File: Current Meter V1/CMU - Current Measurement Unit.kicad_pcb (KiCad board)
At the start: 2 copper layers, 35 parts, among them J401 I2C OLED Display Connector, J501 Connector, U201 MCP6002-xSN, U202 MCP6002-xSN

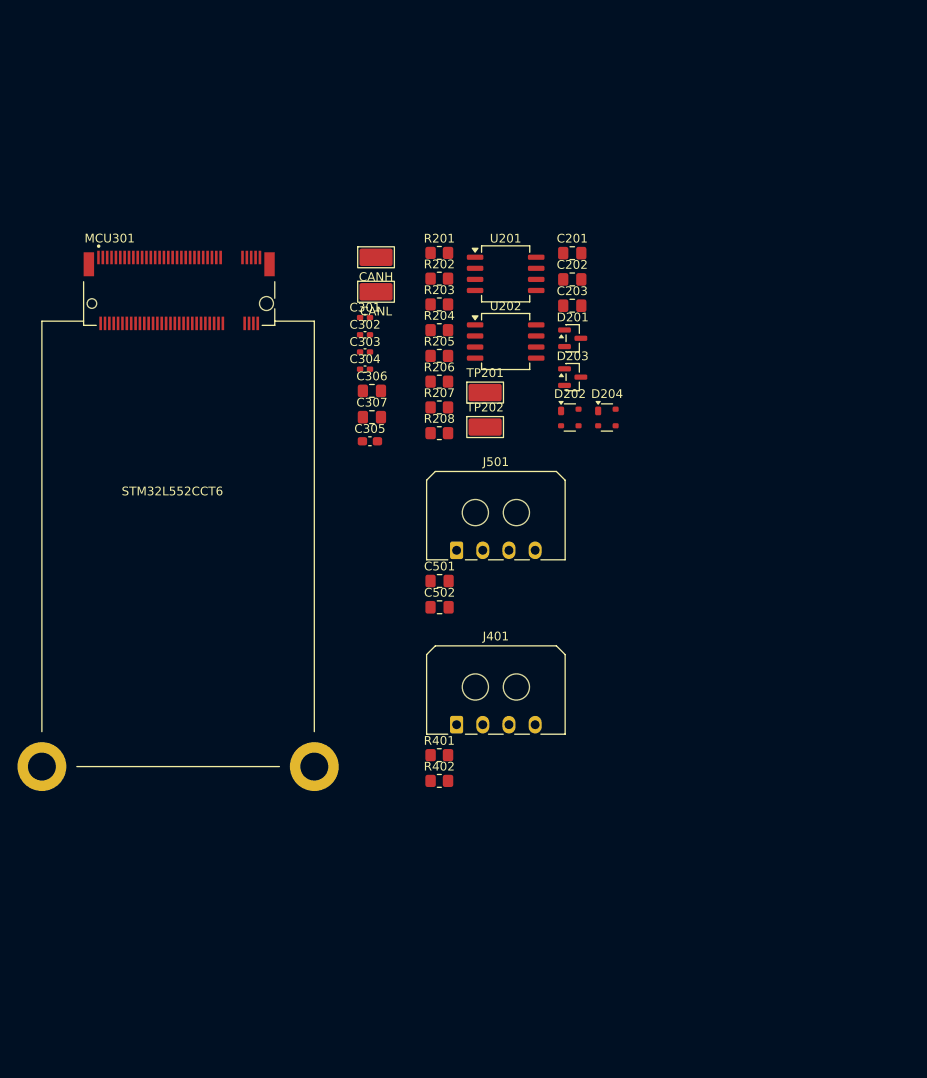
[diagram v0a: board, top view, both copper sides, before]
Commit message: updates
started layout
deleted usb
fully updated op amp footprints
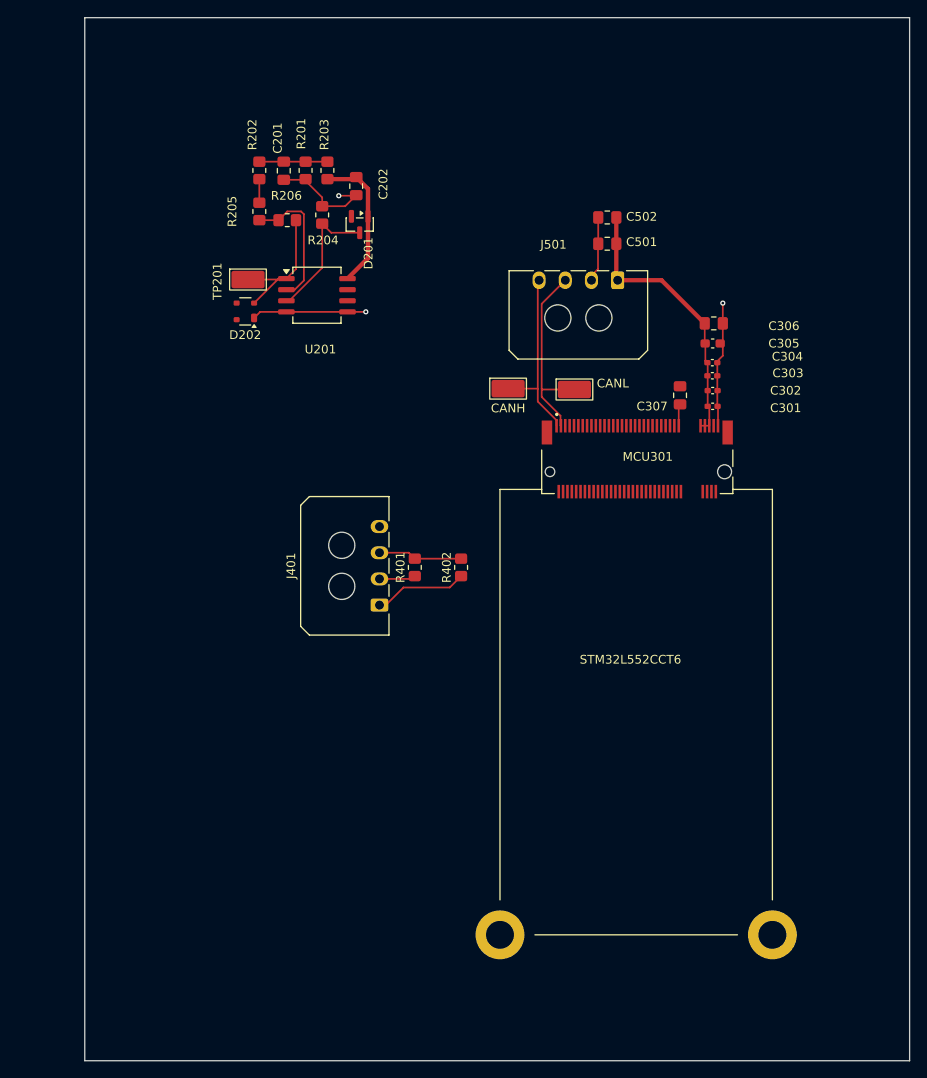
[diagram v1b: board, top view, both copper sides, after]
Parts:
- removed C203: 100n, Capacitor_SMD:C_0805_2012Metric_Pad1.18x1.45mm_HandSolder
- removed D203: BAT54A, Package_TO_SOT_SMD:SOT-23
- removed D204: PRTR5V0U2X, Package_TO_SOT_SMD:SOT-143
- removed R207: 8.2k, Resistor_SMD:R_0805_2012Metric_Pad1.20x1.40mm_HandSolder
- removed R208: 22k, Resistor_SMD:R_0805_2012Metric_Pad1.20x1.40mm_HandSolder
- removed TP202: SMD Test Point, TestPoint:TestPoint_Keystone_5019_Miniature
- removed U202: MCP6002-xSN, Package_SO:SOIC-8_5.3x6.2mm_P1.27mm
- moved MCU301 55.9 mm to (166.2, 92.5)
- moved C502 48.6 mm to (162.8, 64.9), turned to 180 degrees
- moved C501 43.2 mm to (162.8, 67.9), turned to 180 degrees
- moved C301 41.1 mm to (174.8, 86.5)
- moved C305 40.8 mm to (174.8, 79.3)
- moved C302 40.3 mm to (174.8, 84.7)
- moved C306 39.9 mm to (175.0, 77.0)
- moved C303 39.9 mm to (174.8, 83.0)
- moved C304 39.8 mm to (174.8, 81.5)
- moved D202 39.1 mm to (121.3, 75.7), turned to 180 degrees
- moved J501 36.0 mm to (163.9, 72.1), turned to 180 degrees
- moved C307 35.4 mm to (171.1, 85.3), turned to -90 degrees
- moved C201 34.4 mm to (125.7, 59.5), turned to 90 degrees
- moved TP201 30.1 mm to (121.6, 72.0)
- moved D201 27.7 mm to (134.4, 65.7), turned to -90 degrees
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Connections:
- MCU301 pad 45: /opamp/Vout=0.40 Min, 3.278 Max -> /microcontroller/curr_sig
- R205 pad 2: Net-(U202A--) -> Net-(U201A--)
- R206 pad 1: Net-(U202A--) -> Net-(U201A--)
- U201 pad 1: Net-(U201A--) -> /opamp/Gain=0.833, 1.67 (0-3.3)
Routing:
- net GND: track 0.00 -> 50.3 mm, vias 0 -> 3
- net /connector/+5_V: track 0.00 -> 32.2 mm
- net /connector/CAN-: track 0.00 -> 22.5 mm
- net /connector/CAN+: track 0.00 -> 21.0 mm
- net +5V: track 0.00 -> 16.6 mm
- net /opamp/Gain=0.833, 1.67 (0-3.3): track 0.00 -> 16.5 mm
- net Net-(U201A--): track 0.00 -> 15.7 mm
- net /opamp/2.5V, 0.55V-4.5V: track 0.00 -> 15.5 mm
- net /display/I2C_SDA: track 0.00 -> 10.7 mm
- net +3V3: track 0.00 -> 9.63 mm
- net /opamp/0.54V: track 0.00 -> 7.80 mm
- net /display/I2C_SCL: track 0.00 -> 4.18 mm
- net Net-(R202-Pad1): track 0.00 -> 2.70 mm
- added copper zone on In1.Cu, net +5V
- added copper zone on In2.Cu, net GND
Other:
- board outline added: 94.5 x 119.5 mm
- copper layers 2 -> 4

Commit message: buck converter
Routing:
- net GND: track 50.3 -> 50.8 mm, vias 3 -> 5
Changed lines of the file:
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@@
+	)
+	(segment
+		(start 174.95 88.75)
+		(end 175.45 88.75)
+		(width 0.2)
+		(layer "F.Cu")
+		(net 1)
 	)
 	(segment
@@
 		(size 0.6)
 		(drill 0.3)
+		(layers "F.Cu" "B.Cu")
+		(free yes)
+		(net 1)
+	)
+	(via
+		(at 164.2 90.2)
+		(size 0.6)
+		(drill 0.3)
+		(layers "F.Cu" "B.Cu")
+		(free yes)
+		(net 1)
+	)
+	(via
+		(at 174.7 90.5)
+		(size 0.6)
+		(drill 0.3)

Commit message: layup updated
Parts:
- added C601: 10u, Capacitor_SMD:C_0603_1608Metric_Pad1.08x0.95mm_HandSolder, F.Cu at (131.5, 117.9)
- added C602: 10n, Capacitor_SMD:C_0603_1608Metric_Pad1.08x0.95mm_HandSolder, F.Cu at (127.4, 122.8)
- added C603: 220u, Capacitor_THT:CP_Radial_D8.0mm_P3.50mm, F.Cu at (136.1, 134.2)
- added D601: B340, Diode_SMD:D_SMC, F.Cu at (122.8, 123.8)
- added L601: 15u, bfr_inductors:CDRH104RNP-150NC, F.Cu at (126.9, 134.6)
- added R601: 10k, Resistor_SMD:R_0805_2012Metric_Pad1.20x1.40mm_HandSolder, F.Cu at (139.3, 128.2)
- added R602: 3.3k, Resistor_SMD:R_0805_2012Metric_Pad1.20x1.40mm_HandSolder, F.Cu at (139.2, 125.2)
- added SW601: SW_DIP_x01, Button_Switch_SMD:SW_DIP_SPSTx01_Slide_6.7x4.1mm_W6.73mm_P2.54mm_LowProfile_JPin, F.Cu at (138.0, 118.9)
- added U601: TPS5430DDAR, Package_SO:TI_SO-PowerPAD-8_ThermalVias, F.Cu at (131.3, 122.9)
- moved R202 49.8 mm to (136.6, 107.4), turned to -90 degrees
- moved C201 48.5 mm to (133.8, 107.4), turned to -90 degrees
- moved R201 48.0 mm to (131.3, 107.4), turned to -90 degrees
- moved R203 48.0 mm to (128.8, 107.4), turned to 90 degrees
- moved C202 45.1 mm to (125.5, 105.6), turned to 90 degrees
- moved R205 40.9 mm to (136.6, 102.7), turned to 90 degrees
- moved R204 37.7 mm to (129.4, 102.3), turned to 90 degrees
- moved R206 37.3 mm to (133.4, 101.7), turned to 180 degrees
- moved D201 36.7 mm to (125.1, 101.2), turned to 90 degrees
- moved J401 30.1 mm to (129.0, 80.2)
- moved TP201 28.1 mm to (137.9, 94.9), turned to 180 degrees
- moved C502 26.4 mm to (138.3, 74.9), turned to -90 degrees
- moved D202 23.0 mm to (138.2, 91.3), turned to 0 degrees
- moved C501 22.6 mm to (141.3, 74.9), turned to -90 degrees
- moved R401 20.2 mm to (143.8, 85.0)
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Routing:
- net GND: track 50.8 -> 131.1 mm, vias 5 -> 13
- net +3V3: track 9.63 -> 46.9 mm
- net /display/I2C_SCL: track 4.18 -> 34.4 mm
- net /buck/SW_NODE: track 0.00 -> 24.0 mm
- net /display/I2C_SDA: track 10.7 -> 32.6 mm
- net /buck/+5_V: track 0.00 -> 13.6 mm
- net /connector/+5_V: track 32.2 -> 45.5 mm
- net /connector/CAN-: track 22.5 -> 11.4 mm
- net Net-(U601-VSENSE): track 0.00 -> 9.96 mm
- net Net-(U601-EN): track 0.00 -> 5.67 mm
- net /connector/CAN+: track 21.0 -> 15.5 mm
- net Net-(U601-BOOT): track 0.00 -> 2.79 mm
- net /buck/VIN: track 0.00 -> 2.31 mm
- net Net-(U201B--): track 0.00 -> 1.27 mm
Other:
- board size 94.5 x 119.5 mm -> 61.5 x 81.1 mm

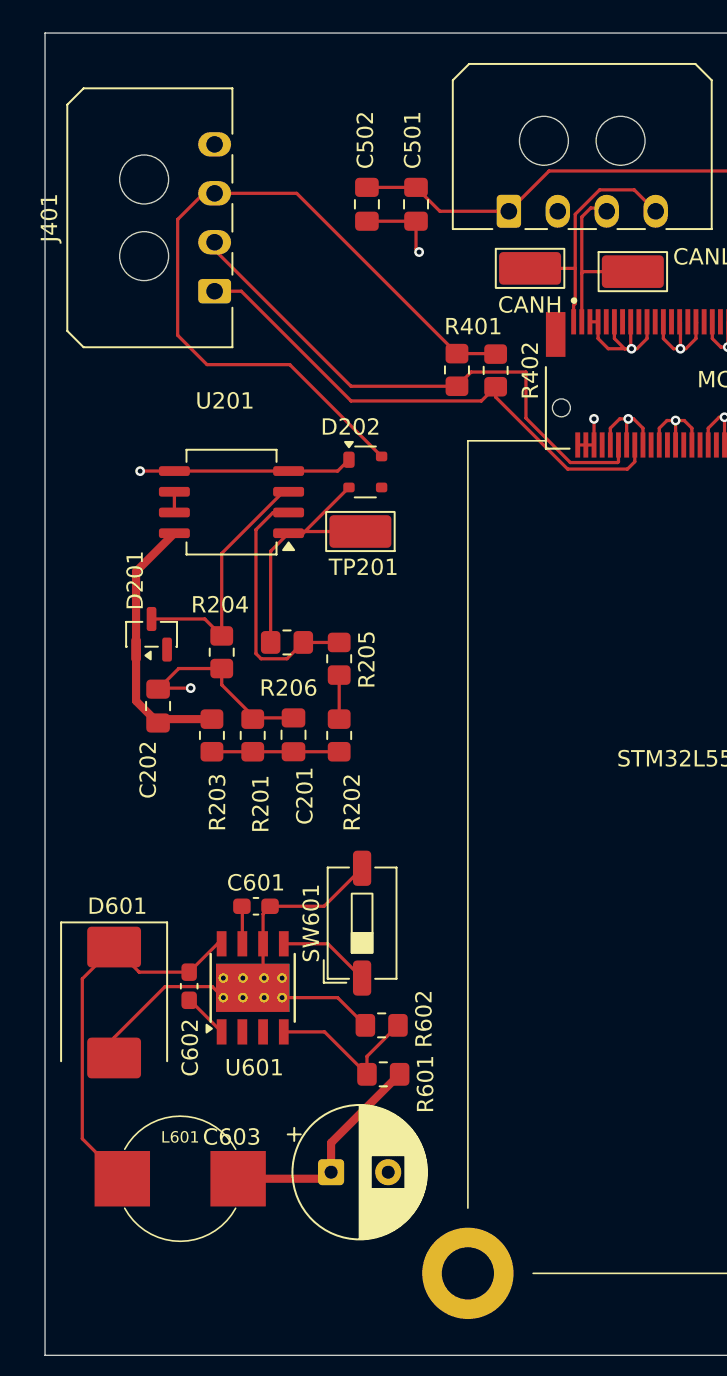
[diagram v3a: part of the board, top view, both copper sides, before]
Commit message: changed everything to 5V
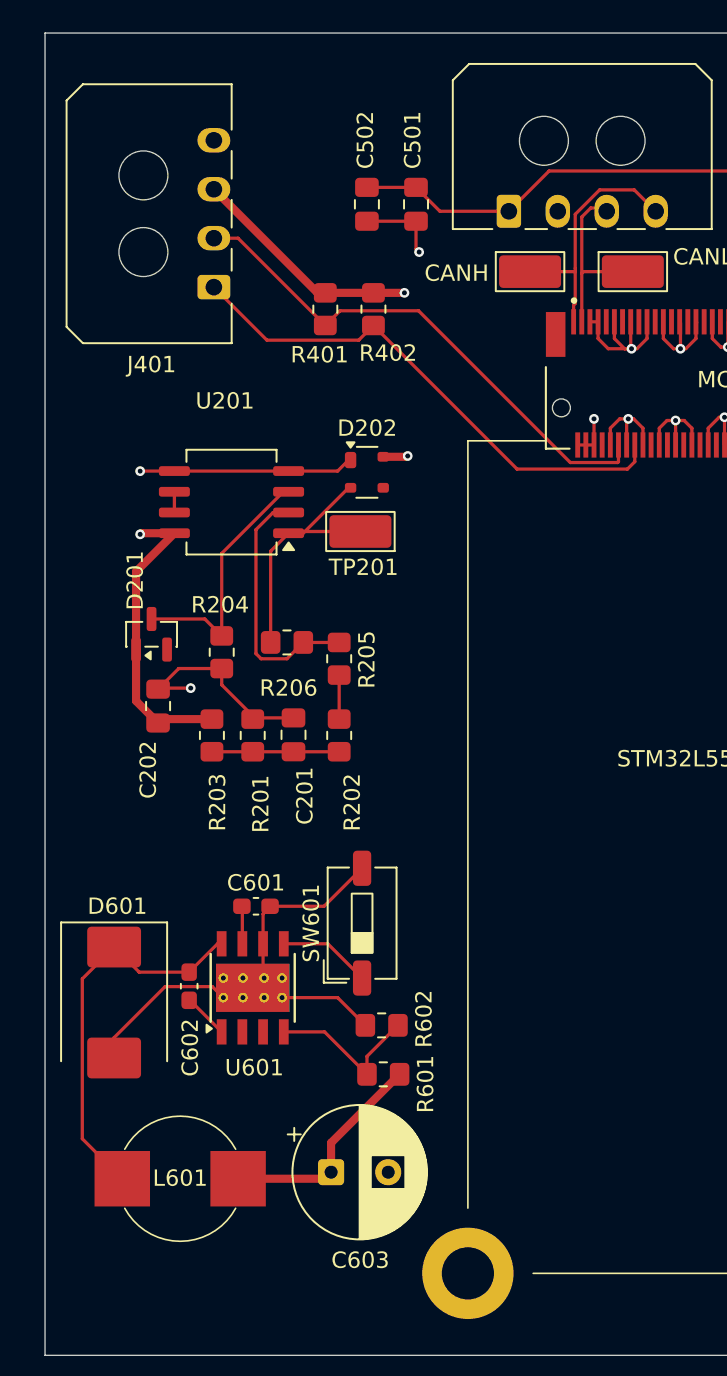
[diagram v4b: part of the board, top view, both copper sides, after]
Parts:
- moved R401 8.89 mm to (135.8, 81.3)
- moved R402 8.38 mm to (138.7, 81.3)
- moved J401 0.25 mm to (128.9, 80.0)
- moved TP301 0.20 mm to (148.3, 79.0)
- moved D202 0.10 mm to (138.3, 91.3)
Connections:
- D202 pad 4: +3V3 -> +5V
- J401 pad 3: +3V3 -> +5V
- R401 pad 2: +3V3 -> +5V
- R402 pad 2: +3V3 -> +5V
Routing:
- net +3V3: track 46.9 -> 0.00 mm
- net +5V: track 16.6 -> 34.5 mm, vias 0 -> 3
- net /display/I2C_SCL: track 34.4 -> 32.3 mm

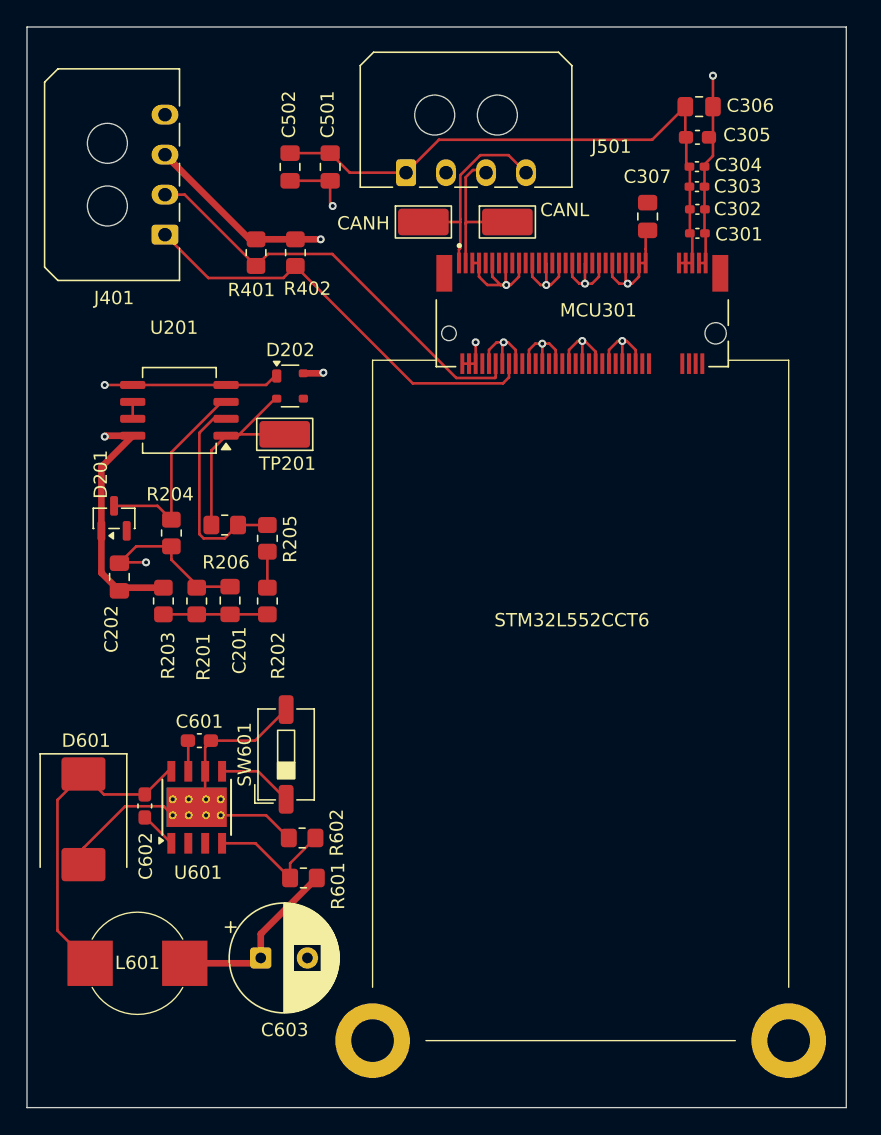
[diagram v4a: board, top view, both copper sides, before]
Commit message: updated layout
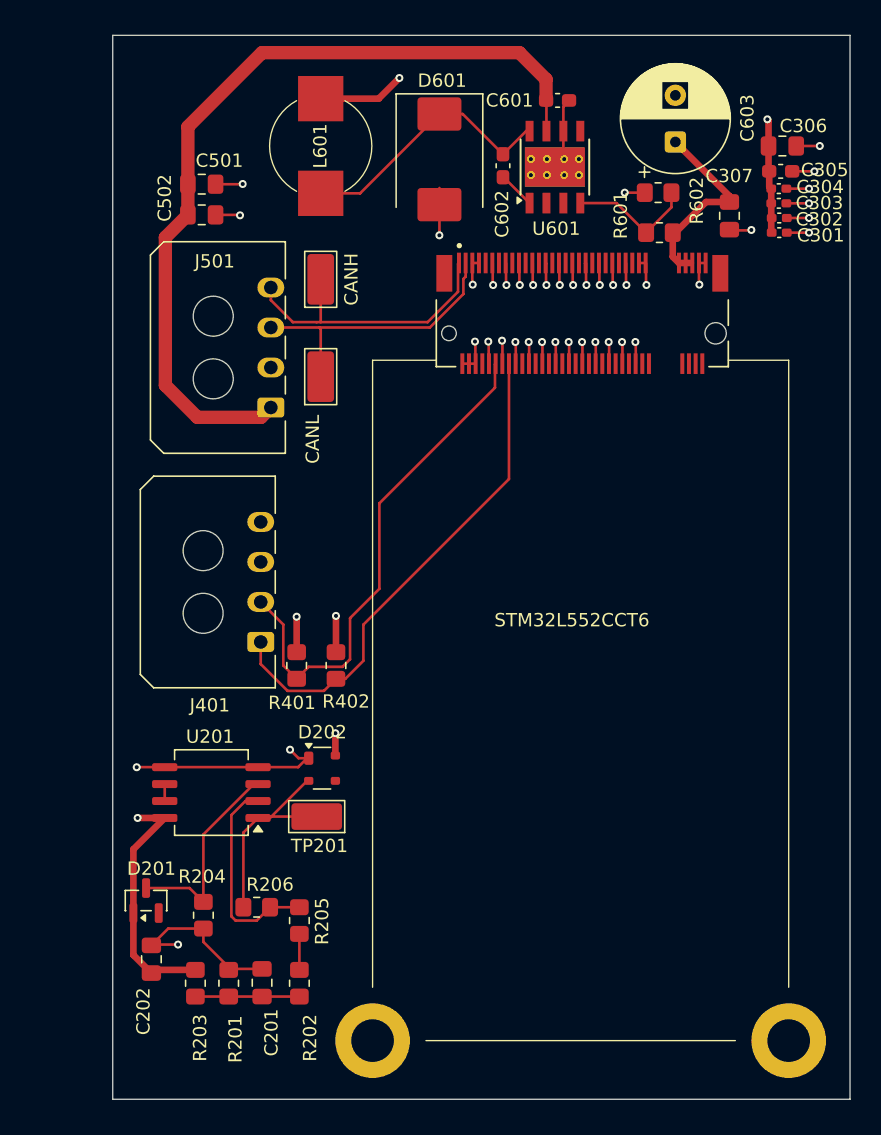
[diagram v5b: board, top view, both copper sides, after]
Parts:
- removed SW601: SW_DIP_x01, Button_Switch_SMD:SW_DIP_SPSTx01_Slide_6.7x4.1mm_W6.73mm_P2.54mm_LowProfile_JPin
- moved C603 68.6 mm to (167.2, 73.0), turned to 90 degrees
- moved L601 62.8 mm to (140.6, 73.3), turned to 90 degrees
- moved D601 56.2 mm to (149.5, 74.3)
- moved R602 55.3 mm to (165.9, 76.8)
- moved R601 55.3 mm to (166.0, 79.8)
- moved C601 55.0 mm to (158.4, 69.9)
- moved U601 55.0 mm to (158.2, 74.9)
- moved C602 55.0 mm to (154.3, 74.8)
- moved J401 31.4 mm to (136.1, 110.5)
- moved R402 31.1 mm to (141.7, 112.3)
- moved R401 31.1 mm to (138.8, 112.3)
- moved D201 28.8 mm to (127.5, 129.9)
- moved R205 28.8 mm to (139.0, 131.4)
- moved R206 28.8 mm to (135.8, 130.4)
- moved R202 28.8 mm to (139.0, 136.1)
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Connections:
- C202 pad 1: +5V -> +5_V
- C301 pad 1: /connector/+5_V -> +5_V
- C302 pad 1: /connector/+5_V -> +5_V
- C303 pad 1: /connector/+5_V -> +5_V
- C304 pad 1: /connector/+5_V -> +5_V
- C305 pad 1: /connector/+5_V -> +5_V
- C306 pad 1: /connector/+5_V -> +5_V
- C307 pad 1: +3.3V -> +5_V
- C501 pad 1: /connector/+5_V -> /buck/+12_V
- C502 pad 1: /connector/+5_V -> /buck/+12_V
- C601 pad 1: /buck/VIN -> /buck/+12_V
- C603 pad 1: /buck/+5_V -> +5_V
- D201 pad 1: +5V -> +5_V
- D202 pad 4: +5V -> +5_V
- J401 pad 3: +5V -> +5_V
- J501 pad 1: /connector/+5_V -> /buck/+12_V
- L601 pad 2: /buck/+5_V -> +5_V
- MCU301 pad 67: /connector/+5_V -> +5_V
- MCU301 pad 69: /connector/+5_V -> +5_V
- MCU301 pad 71: /connector/+5_V -> +5_V
- R203 pad 2: +5V -> +5_V
- R401 pad 2: +5V -> +5_V
- R402 pad 2: +5V -> +5_V
- R601 pad 2: /buck/+5_V -> +5_V
- U201 pad 8: +5V -> +5_V
- U601 pad 5: Net-(U601-EN) -> unconnected-(U601-EN-Pad5)
- U601 pad 7: /buck/VIN -> /buck/+12_V
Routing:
- net /buck/+12_V: track 0.00 -> 63.4 mm
- net +5_V: track 0.00 -> 55.6 mm, vias 0 -> 6
- net /connector/+5_V: track 45.5 -> 0.00 mm
- net +5V: track 34.5 -> 0.00 mm, vias 3 -> 0
- net GND: track 131.1 -> 99.7 mm, vias 13 -> 41
- net /buck/+5_V: track 13.6 -> 0.00 mm
- net /connector/CAN-: track 11.4 -> 21.6 mm
- net /connector/CAN+: track 15.5 -> 22.0 mm
- net /display/I2C_SCL: track 32.3 -> 38.2 mm
- net Net-(U601-EN): track 5.67 -> 0.00 mm
- net /display/I2C_SDA: track 32.4 -> 37.9 mm
- net /buck/SW_NODE: track 24.0 -> 20.1 mm
- net /buck/VIN: track 2.31 -> 0.00 mm
- added copper zone on In2.Cu, net +5_V
- added copper zone on In1.Cu, net GND
- removed copper zone on In1.Cu, net +5V
- removed copper zone on In2.Cu, net GND
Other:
- board size 61.5 x 81.1 mm -> 55.3 x 79.8 mm
